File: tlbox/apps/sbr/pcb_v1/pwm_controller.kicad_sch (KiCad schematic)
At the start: 1 part, among them J1 Conn_01x06_Pin

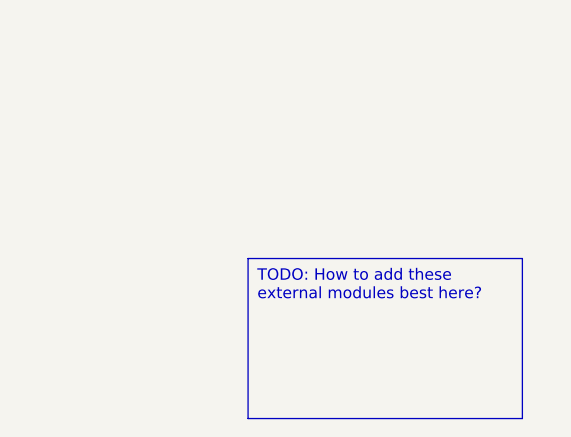
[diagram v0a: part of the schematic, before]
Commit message: update kicad v10
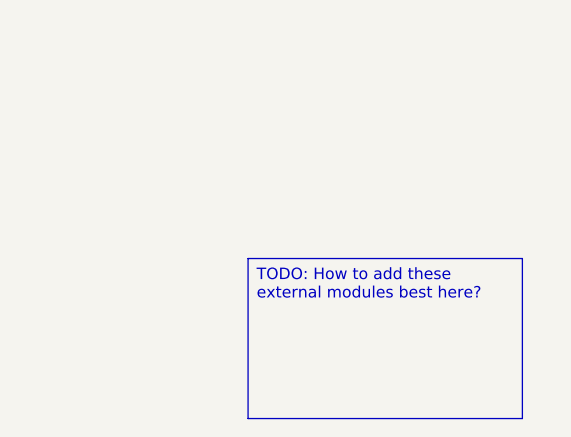
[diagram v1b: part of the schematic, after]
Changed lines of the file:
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@@
-(kicad_sch (version 20230121) (generator eeschema)
-  (paper "A4")
-  (text_box "TODO: How to add these external modules best here?"
-    (at 152.4 99.06 0) (size 30.48 17.78)
-    (stroke (width 0) (type default))
-    (fill (type none))
-    (effects (font (size 1.27 1.27)) (justify left top))
-  )
-  (hierarchical_label "pwm_throttle" (shape output) (at 111.76 68.58 0) (fields_autoplaced)
-    (effects (font (size 1.27 1.27)) (justify left))
-  )
-  (hierarchical_label "pwm_turn" (shape output) (at 111.76 66.04 0) (fields_autoplaced)
-    (effects (font (size 1.27 1.27)) (justify left))
-  )
-  (symbol (lib_id "Connector:Conn_01x06_Pin") (at 106.68 66.04 0) (unit 1)
-    (in_bom yes) (on_board yes) (dnp no) (fields_autoplaced)
-    (property "Reference" "J1" (at 107.315 55.88 0)
-      (effects (font (size 1.27 1.27)))
-    )
-    (property "Value" "Conn_01x06_Pin" (at 107.315 58.42 0)
-      (effects (font (size 1.27 1.27)))
-    )
-    (property "Footprint" "" (at 106.68 66.04 0)
-      (effects (font (size 1.27 1.27)) hide)
-    )
-    (property "Datasheet" "~" (at 106.68 66.04 0)
-      (effects (font (size 1.27 1.27)) hide)
-    )
-    (pin "6")
-    (pin "4")
-    (pin "1")
-    (pin "2")
-    (pin "3")
-    (pin "5")
-    (instances
-      (project "self_balancing_robot_v1"
-        (path "/f1bc52c2-82b2-44ac-a8ec-1286ff19a550/c1d07036-7bde-4d71-93e9-99c260776c4c"
-          (reference "J1") (unit 1)
-        )
-      )
-    )
-  )
+(kicad_sch
+	(version 20260306)
+	(generator "eeschema")
+	(generator_version "10.0")
+	(paper "A4")
+	(text_box "TODO: How to add these external modules best here?"
+		(exclude_from_sim no)
+		(at 152.4 99.06 0)
+		(size 30.48 17.78)
+		(margins 0.9525 0.9525 0.9525 0.9525)
+		(stroke
+			(width 0)
+			(type default)
+		)
+		(fill
+			(type none)
+		)
+		(effects
+			(font
+				(size 1.27 1.27)
+			)
+			(justify left top)
+		)
+	)
+	(hierarchical_label "pwm_throttle"
+		(shape output)
+		(at 111.76 68.58 0)
+		(effects
+			(font
+				(size 1.27 1.27)
+			)
+			(justify left)
+		)
+	)
+	(hierarchical_label "pwm_turn"
+		(shape output)
+		(at 111.76 66.04 0)
+		(effects
+			(font
+				(size 1.27 1.27)
+			)
+			(justify left)
+		)
+	)
+	(symbol
+		(lib_id "Connector:Conn_01x06_Pin")
+		(at 106.68 66.04 0)
+		(unit 1)
+		(body_style 1)
+		(exclude_from_sim no)
+		(in_bom yes)
+		(on_board yes)
+		(in_pos_files yes)
+		(dnp no)
+		(fields_autoplaced yes)
+		(property "Reference" "J1"
+			(at 107.315 55.88 0)
+			(show_name no)
+			(do_not_autoplace no)
+			(effects
+				(font
+					(size 1.27 1.27)
+				)
+			)
+		)
+		(property "Value" "Conn_01x06_Pin"
+			(at 107.315 58.42 0)
+			(show_name no)
+			(do_not_autoplace no)
+			(effects
+				(font
+					(size 1.27 1.27)
+				)
+			)
+		)
+		(property "Footprint" ""
+			(at 106.68 66.04 0)
+			(hide yes)
+			(show_name no)
+			(do_not_autoplace no)
+			(effects
+				(font
+					(size 1.27 1.27)
+				)
+			)
+		)
+		(property "Datasheet" ""
+			(at 106.68 66.04 0)
+			(hide yes)
+			(show_name no)
+			(do_not_autoplace no)
+			(effects
+				(font
+					(size 1.27 1.27)
+				)
+			)
+		)
+		(property "Description" ""
+			(at 106.68 66.04 0)
+			(show_name no)
+			(do_not_autoplace no)
+			(effects
+				(font
+					(size 1.27 1.27)
+				)
+			)
+		)
+		(pin "6"
+		)
+		(pin "4"
+		)
+		(pin "1"
+		)
+		(pin "2"
+		)
+		(pin "3"
+		)
+		(pin "5"
+		)
+		(instances
+			(project "self_balancing_robot_v1"
+				(path "/f1bc52c2-82b2-44ac-a8ec-1286ff19a550/c1d07036-7bde-4d71-93e9-99c260776c4c"
+					(reference "J1")
+					(unit 1)
+				)
+			)
+		)
+	)
 )

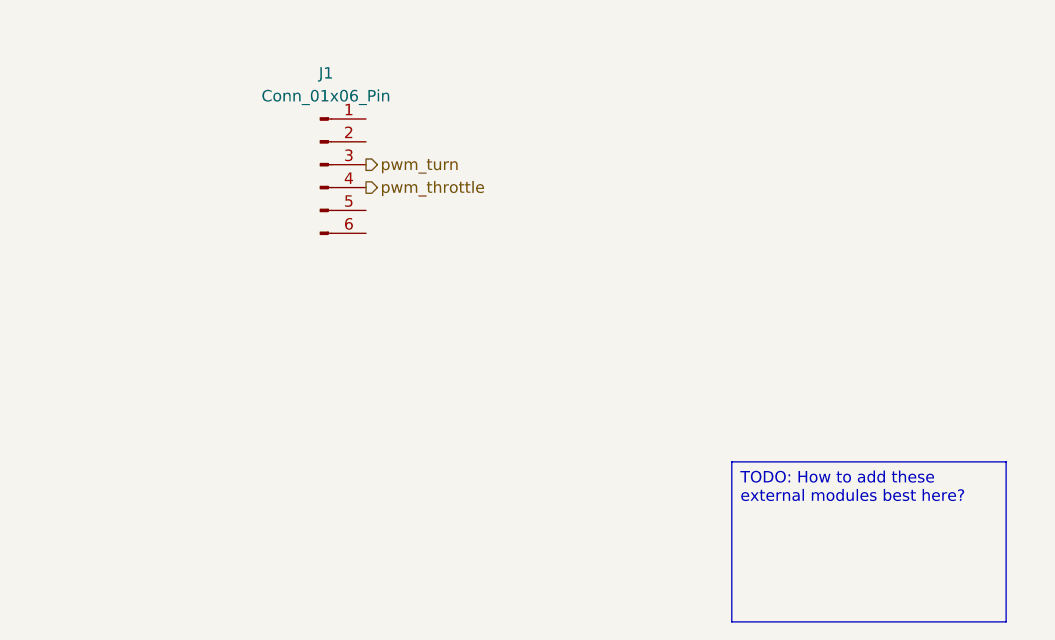
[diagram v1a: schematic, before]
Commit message: New schematic
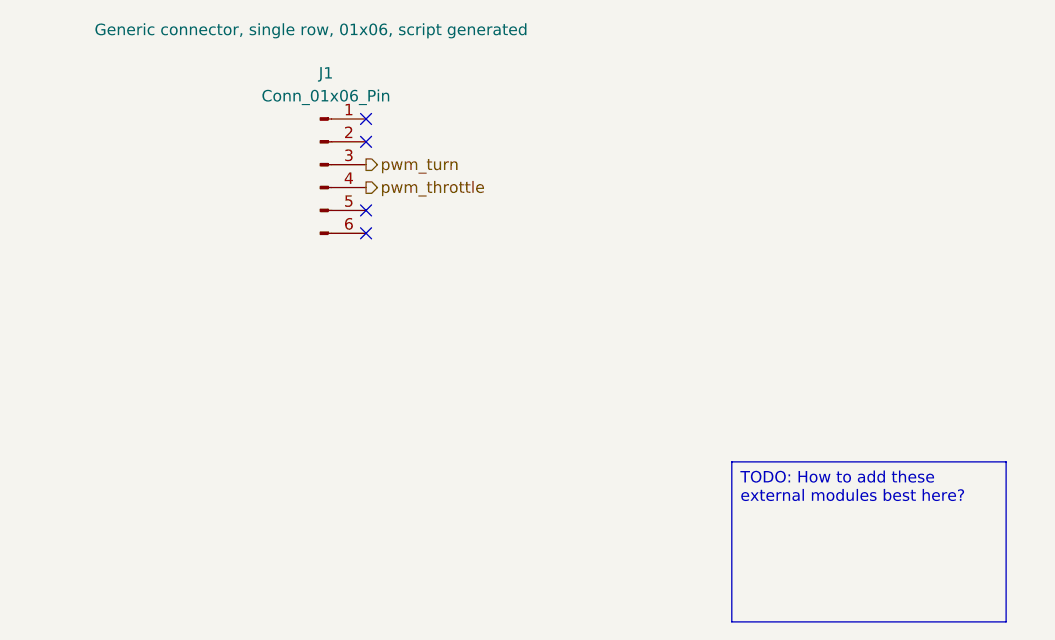
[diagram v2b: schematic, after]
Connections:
- no-connect marks 0 -> 4
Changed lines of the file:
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@@
 		)
+	)
+	(no_connect
+		(at 111.76 63.5)
+	)
+	(no_connect
+		(at 111.76 73.66)
+	)
+	(no_connect
+		(at 111.76 71.12)
+	)
+	(no_connect
+		(at 111.76 60.96)
 	)
 	(hierarchical_label "pwm_throttle"
@@
 		(in_pos_files yes)
 		(dnp no)
-		(fields_autoplaced yes)
 		(property "Reference" "J1"
 			(at 107.315 55.88 0)
@@
 			)
 		)
-		(property "Description" ""
-			(at 106.68 66.04 0)
+		(property "Description" "Generic connector, single row, 01x06, script generated"
+			(at 105.664 51.054 0)
 			(show_name no)
 			(do_not_autoplace no)
